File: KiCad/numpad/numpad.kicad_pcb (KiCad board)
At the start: 2 copper layers, 19 parts, among them J1 Barrel_Jack_Switch, J10 Conn_01x02_Pin, J2 Conn_01x03_Pin, J3 Conn_01x04_Pin, J4 Conn_01x05_Pin, J5 Conn_01x06_Pin, J6 Conn_01x07_Pin, J7 Conn_01x08_Pin, J8 Conn_01x09_Pin, J9 Conn_01x10_Pin, SW1 Cherry Switch Single, SW2 Cherry Switch 1.5x - Enter Key, U2 TMC2209, U3 Display, U4 ICM-20948, U5 24LC512, U6 Adafruit_ICM20948, U7 LTV-817S

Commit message: PCB designs started
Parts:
- removed J10: Conn_01x02_Pin, Connector_JST:JST_PH_B2B-PH-K_1x02_P2.00mm_Vertical
- removed J2: Conn_01x03_Pin, Connector_JST:JST_PH_B3B-PH-K_1x03_P2.00mm_Vertical
- removed J3: Conn_01x04_Pin, Connector_JST:JST_PH_B4B-PH-K_1x04_P2.00mm_Vertical
- removed J4: Conn_01x05_Pin, Connector_JST:JST_PH_B5B-PH-K_1x05_P2.00mm_Vertical
- removed J5: Conn_01x06_Pin, Connector_JST:JST_PH_B6B-PH-K_1x06_P2.00mm_Vertical
- removed J6: Conn_01x07_Pin, Connector_JST:JST_PH_B7B-PH-K_1x07_P2.00mm_Vertical
- removed J7: Conn_01x08_Pin, Connector_JST:JST_PH_B8B-PH-K_1x08_P2.00mm_Vertical
- removed J8: Conn_01x09_Pin, Connector_JST:JST_PH_B9B-PH-K_1x09_P2.00mm_Vertical
- removed J9: Conn_01x10_Pin, Connector_JST:JST_PH_B10B-PH-K_1x10_P2.00mm_Vertical
- removed U3: Display, ComponentLib:NHD-2.23-12832UCB3
- removed U4: ICM-20948, ComponentLib:ICM-20948
- removed U5: 24LC512, Package_SO:SOIC-8_5.3x6.2mm_P1.27mm
- removed U6: Adafruit_ICM20948, ComponentLib:Adafruit-ICM-20948
- removed U7: LTV-817S, Package_DIP:SMDIP-4_W9.53mm
- added C1: C, Capacitor_SMD:C_0603_1608Metric_Pad1.08x0.95mm_HandSolder, B.Cu at (165.4, 64.0)
- added C2: C, Capacitor_SMD:C_0603_1608Metric_Pad1.08x0.95mm_HandSolder, B.Cu at (152.5, 62.4)
- added C3: 1n, Capacitor_SMD:C_0603_1608Metric, B.Cu at (134.3, 60.0)
- added D1: LED, Diode_SMD:D_0603_1608Metric, B.Cu at (132.0, 64.0)
- added H1: MountingHole, MountingHole:MountingHole_3.2mm_M3, F.Cu at (110.5, 60.0)
- added H2: MountingHole, MountingHole:MountingHole_3.2mm_M3, F.Cu at (175.5, 60.0)
- added H3: MountingHole, MountingHole:MountingHole_3.2mm_M3, F.Cu at (110.5, 147.4)
- added H4: MountingHole, MountingHole:MountingHole_3.2mm_M3, F.Cu at (175.5, 147.5)
- added R1: 1k, Resistor_SMD:R_0603_1608Metric, B.Cu at (125.7, 62.8)
- added R10: 1k, Resistor_SMD:R_0603_1608Metric, B.Cu at (171.7, 67.0)
- added R11: 1k, Resistor_SMD:R_0603_1608Metric, B.Cu at (131.7, 87.0)
- added R12: 1k, Resistor_SMD:R_0603_1608Metric, B.Cu at (151.8, 87.0)
- added R13: 1k, Resistor_SMD:R_0603_1608Metric, B.Cu at (171.7, 87.0)
- added R14: 1k, Resistor_SMD:R_0603_1608Metric, B.Cu at (131.8, 107.0)
- added R15: 1k, Resistor_SMD:R_0603_1608Metric, B.Cu at (151.8, 107.0)
- added R16: 1k, Resistor_SMD:R_0603_1608Metric, B.Cu at (171.8, 107.0)
- added R17: 1k, Resistor_SMD:R_0603_1608Metric, B.Cu at (151.8, 127.0)
- added R18: 1k, Resistor_SMD:R_0603_1608Metric, B.Cu at (151.8, 130.2)
- added R19: 100k, Resistor_SMD:R_0603_1608Metric, B.Cu at (127.8, 60.0)
- added R2: 10k, Resistor_SMD:R_0603_1608Metric, B.Cu at (122.5, 62.8)
- added R20: 1k, Resistor_SMD:R_0603_1608Metric, B.Cu at (131.0, 60.0)
- added R21: 4k7, Resistor_SMD:R_0603_1608Metric, B.Cu at (135.5, 64.0)
- added R3: 51k, Resistor_SMD:R_0603_1608Metric, B.Cu at (119.4, 62.8)
- added R4: 0R, Resistor_SMD:R_0603_1608Metric, B.Cu at (164.5, 61.5)
- added R5: 0R, Resistor_SMD:R_0603_1608Metric, B.Cu at (154.5, 62.5)
- added R6: 100R, Resistor_SMD:R_0603_1608Metric, B.Cu at (150.1, 62.8)
- added R7: 100R, Resistor_SMD:R_0603_1608Metric, B.Cu at (150.1, 60.8)
- added R8: 7k5, Resistor_SMD:R_0603_1608Metric, B.Cu at (122.5, 61.0)
- added R9: 1k, Resistor_SMD:R_0603_1608Metric, B.Cu at (151.7, 67.0)
- added SW10: Cherry Switch Single, ComponentLib:SW_Cherry_MX_1.00u_PCB, F.Cu at (143.1, 135.0)
- added SW3: Cherry Switch Single, ComponentLib:SW_Cherry_MX_1.00u_PCB, F.Cu at (163.0, 75.0)
- added SW4: Cherry Switch Single, ComponentLib:SW_Cherry_MX_1.00u_PCB, F.Cu at (123.0, 95.0)
- added SW5: Cherry Switch Single, ComponentLib:SW_Cherry_MX_1.00u_PCB, F.Cu at (143.1, 95.0)
- added SW6: Cherry Switch Single, ComponentLib:SW_Cherry_MX_1.00u_PCB, F.Cu at (163.0, 95.0)
- added SW7: Cherry Switch Single, ComponentLib:SW_Cherry_MX_1.00u_PCB, F.Cu at (123.0, 115.0)
- added SW8: Cherry Switch Single, ComponentLib:SW_Cherry_MX_1.00u_PCB, F.Cu at (143.1, 115.0)
- added SW9: Cherry Switch Single, ComponentLib:SW_Cherry_MX_1.00u_PCB, F.Cu at (163.0, 115.0)
- added TP1: TestPoint, TestPoint:TestPoint_Pad_D2.0mm, B.Cu at (124.2, 67.6)
- added TP2: TestPoint, TestPoint:TestPoint_Pad_D2.0mm, B.Cu at (154.6, 58.8)
- J1: value Barrel_Jack_Switch -> Conn_01x04_Pin; footprint Connector_BarrelJack:BarrelJack_Wuerth_694106106102_2.0x5.5mm -> Connector_JST:JST_PH_B4B-PH-K_1x04_P2.00mm_Vertical; moved to B.Cu
- SW2: value Cherry Switch 1.5x - Enter Key -> Cherry Switch Single; footprint ComponentLib:SW_Cherry_MX_1.50u_PCB -> ComponentLib:SW_Cherry_MX_1.00u_PCB
- U1: value ~ -> LT1632; footprint ComponentLib:NUCLEO-F767ZI -> Package_SO:SOIC-8_3.9x4.9mm_P1.27mm; moved to B.Cu
- U2: value TMC2209 -> TL431D; footprint ComponentLib:TMC2209 Silentstepstick -> Package_SO:SOIC-8_3.9x4.9mm_P1.27mm; moved to B.Cu
- moved U1 242.8 mm to (159.5, 62.5), turned to 180 degrees
- moved U2 159.4 mm to (119.8, 67.3), turned to 90 degrees
- moved SW2 95.9 mm to (143.0, 75.0)
- moved SW1 75.9 mm to (123.0, 75.0)
- moved J1 67.2 mm to (140.0, 62.6)
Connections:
- J1 pad 1: unconnected-(J1-Pad1) -> +5V
- J1 pad 2: unconnected-(J1-Pad2) -> /NUMPAD_VREF
- J1 pad 3: unconnected-(J1-Pad3) -> /NUMPAD_A_OUT
- SW1 pad 1: unconnected-(SW1-Pad1) -> /3Vref
- SW1 pad 2: unconnected-(SW1-Pad2) -> Net-(R19-Pad1)
- SW2 pad 1: unconnected-(SW2-Pad1) -> Net-(R10-Pad1)
- SW2 pad 2: unconnected-(SW2-Pad2) -> Net-(R19-Pad1)
- U2 pad 1: unconnected-(U2-Dir-Pad1) -> /3Vref
- U2 pad 2: unconnected-(U2-Step-Pad2) -> GND
- U2 pad 3: unconnected-(U2-PDN/UART-Pad3) -> GND
- U2 pad 4: unconnected-(U2-PDN/UART-Pad4) -> (no net)
- U2 pad 5: unconnected-(U2-SPREAD-Pad5) -> (no net)
- U2 pad 6: unconnected-(U2-MS2-Pad6) -> GND
- U2 pad 7: unconnected-(U2-MS1-Pad7) -> GND
- U2 pad 8: unconnected-(U2-EN-Pad8) -> Net-(U2-REF)
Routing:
- net Net-(R19-Pad1): track 0.00 -> 230.3 mm
- net Net-(R10-Pad2): track 0.00 -> 47.6 mm
- net Net-(R13-Pad2): track 0.00 -> 47.5 mm
- net /3Vref: track 0.00 -> 41.3 mm
- net +5V: track 0.00 -> 34.8 mm
- net /NumpadOut: track 0.00 -> 34.3 mm
- net Net-(R16-Pad2): track 0.00 -> 34.0 mm
- net Net-(R14-Pad2): track 0.00 -> 27.8 mm
- net Net-(R11-Pad2): track 0.00 -> 27.8 mm
- net Net-(R10-Pad1): track 0.00 -> 27.7 mm
- net Net-(R15-Pad2): track 0.00 -> 27.7 mm
- net Net-(R12-Pad2): track 0.00 -> 27.6 mm
- net Net-(U1A-OUT_A): track 0.00 -> 18.2 mm
- net /NUMPAD_VREF: track 0.00 -> 8.62 mm
- net Net-(R17-Pad2): track 0.00 -> 8.30 mm
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- added copper zone on B.Cu, net /3Vref
- added copper zone on B.Cu, net GND
- added copper zone on F.Cu, net GND
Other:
- board outline added: 75 x 97.5 mm

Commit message: numpad, buttons, display PCB done, review needed
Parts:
- moved R6 0.72 mm to (150.2, 63.5)
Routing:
- net Net-(U1A-OUT_A): track 18.2 -> 17.5 mm
- net GND: vias 0 -> 267
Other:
- board text added: "0"
- board text added: "1"
- board text added: "2"
- board text added: "3"
- board text added: "4"
- board text added: "5"
- board text added: "6"
- board text added: "7"
- board text added: "8"
- board text added: "9"

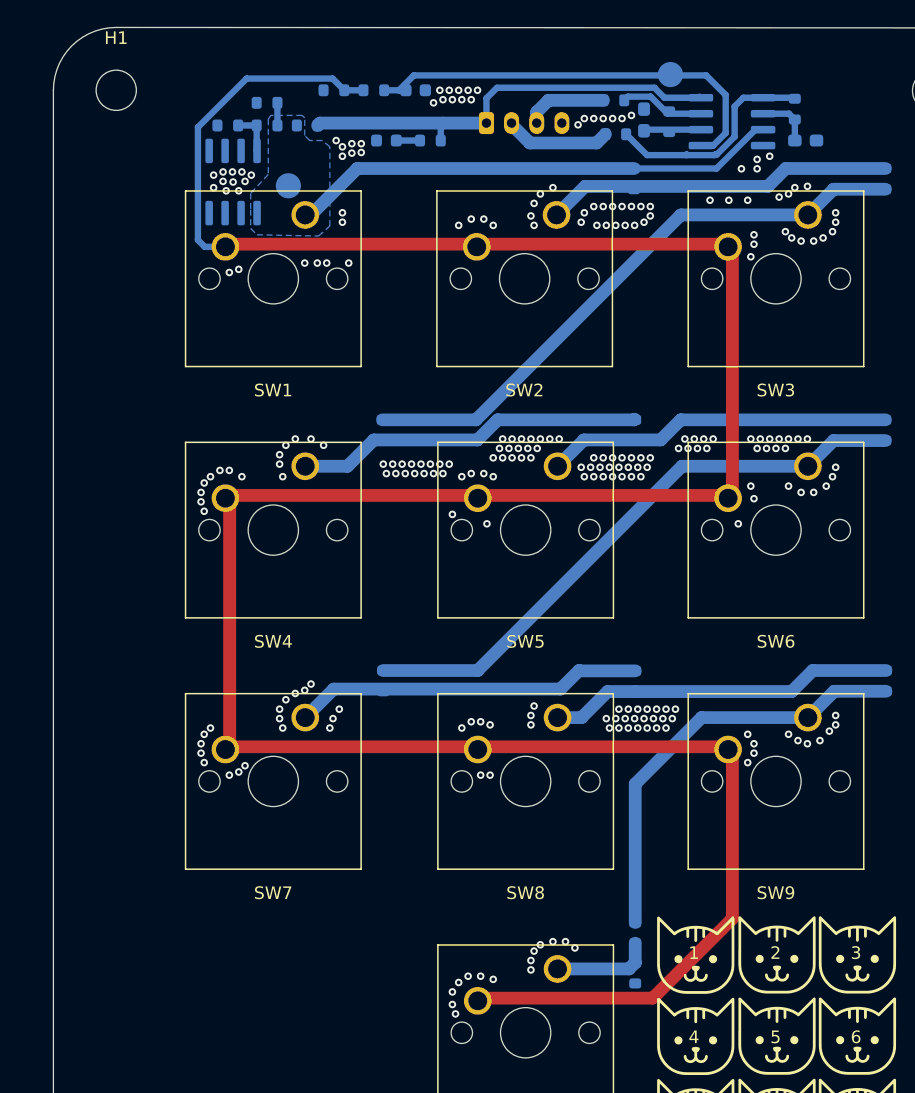
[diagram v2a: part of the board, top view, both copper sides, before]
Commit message: PCB bugfixes based on review
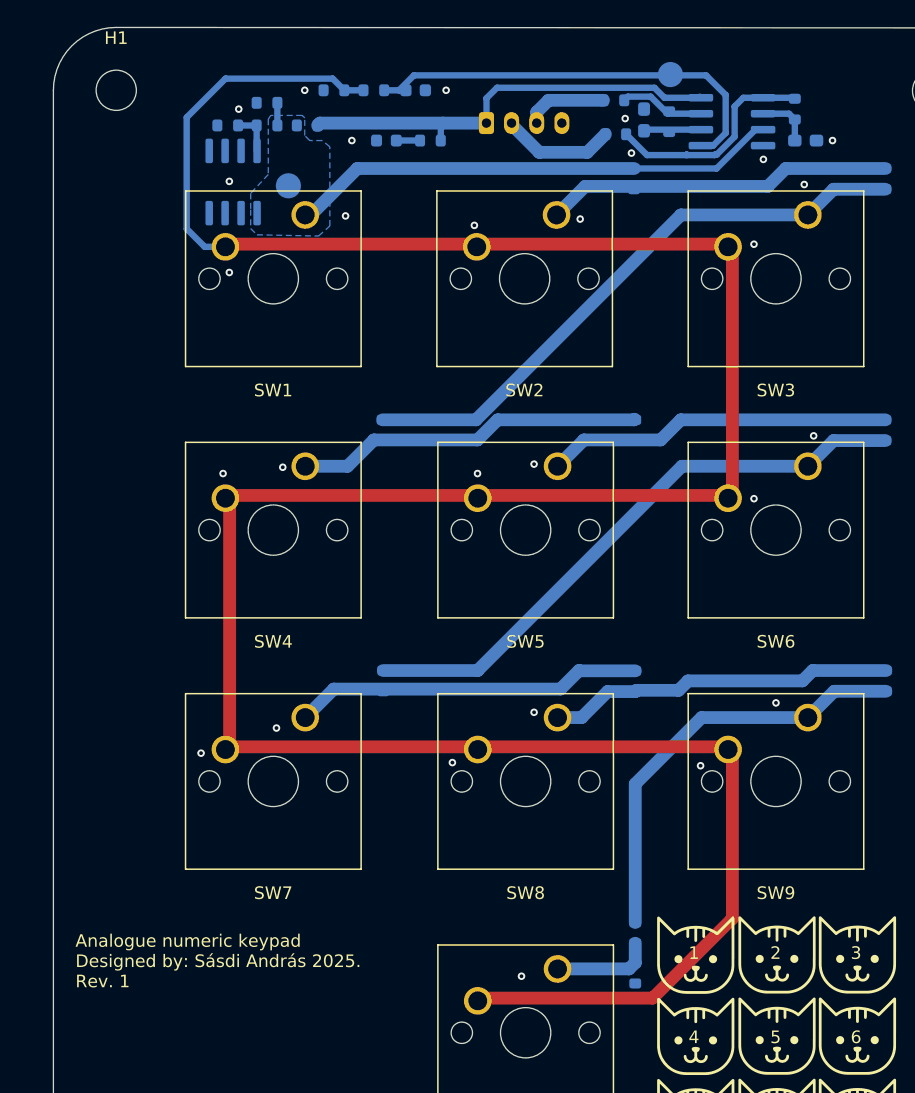
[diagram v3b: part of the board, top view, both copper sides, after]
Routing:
- net Net-(R19-Pad1): track 230.3 -> 221.4 mm
- net /3Vref: track 41.3 -> 40.0 mm
- net GND: vias 267 -> 28
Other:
- board text added: "+5V"
- board text added: "A_OUT"
- board text added: "Analogue numeric keypad Designed by: Sásdi András 2025. Rev. 1"
- board text added: "GND"
- board text added: "VREF_OUT"
